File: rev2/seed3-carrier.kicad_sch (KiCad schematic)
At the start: 48 parts, among them J1 AudioJack2_Switch, J2 AudioJack2, J3 5V_IN, J4 DISPLAY_UART, J5 SJ1-3535NG, J6 Seed3_PINS_RIGHT, J7 Seed3_PINS_LEFT, Q1 AO3401A, U1 TLV9062IDR, U2 TPA6111A2DR

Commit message: Replace rev 2 pots with a volume encoder and add a watchdog output mute
- Remove RV1-RV3, C10, C11. R17 (1M to VREF) keeps the guitar input load;
  input trim and tone move to firmware.
- Add SW1 rotary encoder with push switch and RC conditioning on ENC_A/B/SW
  (Daisy pins 22/23/24).
- Add U3 (SN74LVC1G123) + Q2: U2 SHUTDOWN is pulled to +5V (muted) unless the
  firmware toggles AUDIO_ALIVE (pin 33) every audio callback; ~10 ms timeout.
- Add rev2/CHANGES.md listing these changes, firmware impact and open items.

Co-Authored-By: Claude Opus 5.5 <noreply@anthropic.com>
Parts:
- removed C10, C11: 100nF, Capacitor_SMD:C_1206_3216Metric_Pad1.33x1.80mm_HandSolder, symbol Device:C_Small
- removed RV1: 1M INPUT LEVEL, Seed3_Carrier:Potentiometer_Bourns_PTV09A-4_Single_Vertical_3mmMount, symbol Device:R_Potentiometer_Small
- removed RV2, RV3: 10k linear, Seed3_Carrier:Potentiometer_Bourns_PTV09A-4_Single_Vertical_3mmMount, symbol Device:R_Potentiometer_Small
- added C19, C20, C21: 10nF, Capacitor_SMD:C_1206_3216Metric_Pad1.33x1.80mm_HandSolder, symbol Device:C_Small
- added C22, C23: 100nF, Capacitor_SMD:C_1206_3216Metric_Pad1.33x1.80mm_HandSolder, symbol Device:C_Small
- added Q2: 2N7002, Package_TO_SOT_SMD:SOT-23, symbol Transistor_FET:2N7002
- added R17: 1M, Resistor_SMD:R_1206_3216Metric_Pad1.30x1.75mm_HandSolder, symbol Device:R_Small_US
- added R18, R19, R20, R21, R22, R23: 10k, Resistor_SMD:R_1206_3216Metric_Pad1.30x1.75mm_HandSolder, symbol Device:R_Small_US
- added R24, R25, R26, R27: 100k, Resistor_SMD:R_1206_3216Metric_Pad1.30x1.75mm_HandSolder, symbol Device:R_Small_US
- added SW1: EC11E, Rotary_Encoder:RotaryEncoder_Alps_EC11E-Switch_Vertical_H20mm, symbol Device:RotaryEncoder_Switch
- added TP10: TP_SHDN, TestPoint:TestPoint_Pad_D2.0mm, symbol Connector:TestPoint
- added U3: SN74LVC1G123DCTR, Package_SO:SSOP-8_2.95x2.8mm_P0.65mm, symbol 74xGxx:74LVC1G123
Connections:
- net +5V: now also R27.1
- net 3V3_D: now also C23.1, R18.1, R20.1, R22.1, R24.1, U3.3 (~{CLR}), U3.8 (VCC)
- net GND: now also C19.2, C20.2, C21.2, C23.2, Q2.2 (S), R25.2, R26.2, SW1.C, SW1.S1, U3.1 (~{A}), U3.4 (GND); no longer U2.5 (SHDN)
- net VREF: now also R17.2
- net at R1.1: now also C3.2, R17.1
- net A2 renamed ENC_SW
- net ENC_SW: now also C21.1, R23.2
- net D26 renamed AUDIO_ALIVE
- net AUDIO_ALIVE: now also R25.1, U3.2 (B)
- net TONE_POT renamed ENC_B
- net ENC_B: now also C20.1, R21.2
- net VOLUME_POT renamed ENC_A
- net ENC_A: now also C19.1, R19.2
- new net: C22.1, U3.6 (Cext)
- new net: C22.2, R24.2, U3.7 (RCext)
- new net: Q2.1 (G), R26.1, U3.5 (Q)
- new net AMP_SHUTDOWN: Q2.3 (D), R27.2, TP10.1, U2.5 (SHDN)
- new net ENC_A_RAW: R18.2, R19.1, SW1.A
- new net ENC_B_RAW: R20.2, R21.1, SW1.B
- new net ENC_SW_RAW: R22.2, R23.1, SW1.S2
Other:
- note added: "Amps stay muted (SHUTDOWN pulled to +5V) unless the firmware toggles AUDIO_ALIVE from the audio callback. Each rising edge retriggers U3; if edges stop for ~10 ms (Rext x Cext), Q falls, Q2 turns off and the amps mute. Also muted while the Daisy is absent, booting or in DFU (B is held low). Wire the rev 2 speaker amp mute to AMP_SHUTDOWN."
- note added: "Master volume: rotary encoder, push = mute. 10k pull-up, 10k series, 10nF per encoder vendor app notes."
- note added: "OUTPUT MUTE WATCHDOG"
- note added: "R17 = 1M guitar input load. No input level pot: trim gain in firmware."
- note removed: "RV1: CW = full level. Turn down for hot pickups/pedals."

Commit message: Feed the speaker from AUDIO_OUT_2 and detect headphones in firmware
- Drop the J5 tip-switch line out; TN/RN are now no-connects.
- Add AUDIO_OUT_2 -> RC filter -> U1C buffer -> C26 -> LINE_SEND -> J2.
- Swap U1 to a TLV9064 quad (SOIC-14); U1D parked as a VREF follower for
  the future AUX input buffer.
- Add HP_DETECT on Daisy pin 34 (was D27) with pull-up, series R, filter
  cap and TP11; J5 still needs a jack with an isolated detect switch.
- Update rev2/CHANGES.md.

Co-Authored-By: Claude Opus 5.5 <noreply@anthropic.com>
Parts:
- added C24: 1nF, Capacitor_SMD:C_1206_3216Metric_Pad1.33x1.80mm_HandSolder, symbol Device:C_Small
- added C25: 1uF, Capacitor_SMD:C_1206_3216Metric_Pad1.33x1.80mm_HandSolder, symbol Device:C_Small
- added C26: 10uF, Capacitor_SMD:C_1206_3216Metric_Pad1.33x1.80mm_HandSolder, symbol Device:C_Small
- added C27: 100nF, Capacitor_SMD:C_1206_3216Metric_Pad1.33x1.80mm_HandSolder, symbol Device:C_Small
- added R28: 3.3k, Resistor_SMD:R_1206_3216Metric_Pad1.30x1.75mm_HandSolder, symbol Device:R_Small_US
- added R29: 1M, Resistor_SMD:R_1206_3216Metric_Pad1.30x1.75mm_HandSolder, symbol Device:R_Small_US
- added R30: 10k, Resistor_SMD:R_1206_3216Metric_Pad1.30x1.75mm_HandSolder, symbol Device:R_Small_US
- added R31: 1k, Resistor_SMD:R_1206_3216Metric_Pad1.30x1.75mm_HandSolder, symbol Device:R_Small_US
- added TP11: TP_HP_DET, TestPoint:TestPoint_Pad_D2.0mm, symbol Connector:TestPoint
- added unit 4 of U1
- added unit 3 of U1
- U1: value TLV9062IDR -> TLV9064IDR; footprint Package_SO:SOIC-8_3.9x4.9mm_P1.27mm -> Package_SO:SOIC-14_3.9x8.7mm_P1.27mm; symbol Amplifier_Operational:TL072 -> Amplifier_Operational:TL074
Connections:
- net +5V: now also U1.4 (V+); no longer U1.8 (V+)
- net 3V3_D: now also R30.1
- net AUDIO_OUT_2: now also R28.1
- net GND: now also U1.11 (V-), C24.2, C27.2; no longer U1.4 (V-)
- net LINE_SEND: now also C26.2; no longer J5.TN
- net VREF: now also R29.1, U1.12 (+)
- net D27 renamed HP_DETECT
- net HP_DETECT: now also C27.1, R30.2, R31.2
- new net: U1.13 (-), U1.14
- new net: C24.1, C25.1, R28.2
- new net: C25.2, R29.2, U1.10 (+)
- new net: C26.1, U1.8, U1.9 (-)
- new net HP_DETECT_SW: R31.1, TP11.1
- no-connect marks 2 -> 3
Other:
- note added: "AUDIO_OUT_2 feeds the speaker amp / J2 independently of the headphones. Firmware sets its level and mutes it when HP_DETECT shows headphones are in. U1D is a spare, parked as a VREF follower: use it for the AUX input buffer."
- note added: "Headphone detect: J5 needs a jack with an isolated detect switch (part TBD). Wire it between HP_DETECT_SW and GND. Bring-up: short TP11 to GND to simulate headphones."
- note added: "SPEAKER / LINE SEND"
- note removed: "Line out: J2 is fed from HP_L through J5's tip switch (LINE_SEND). Plugging headphones into J5 mutes J2."

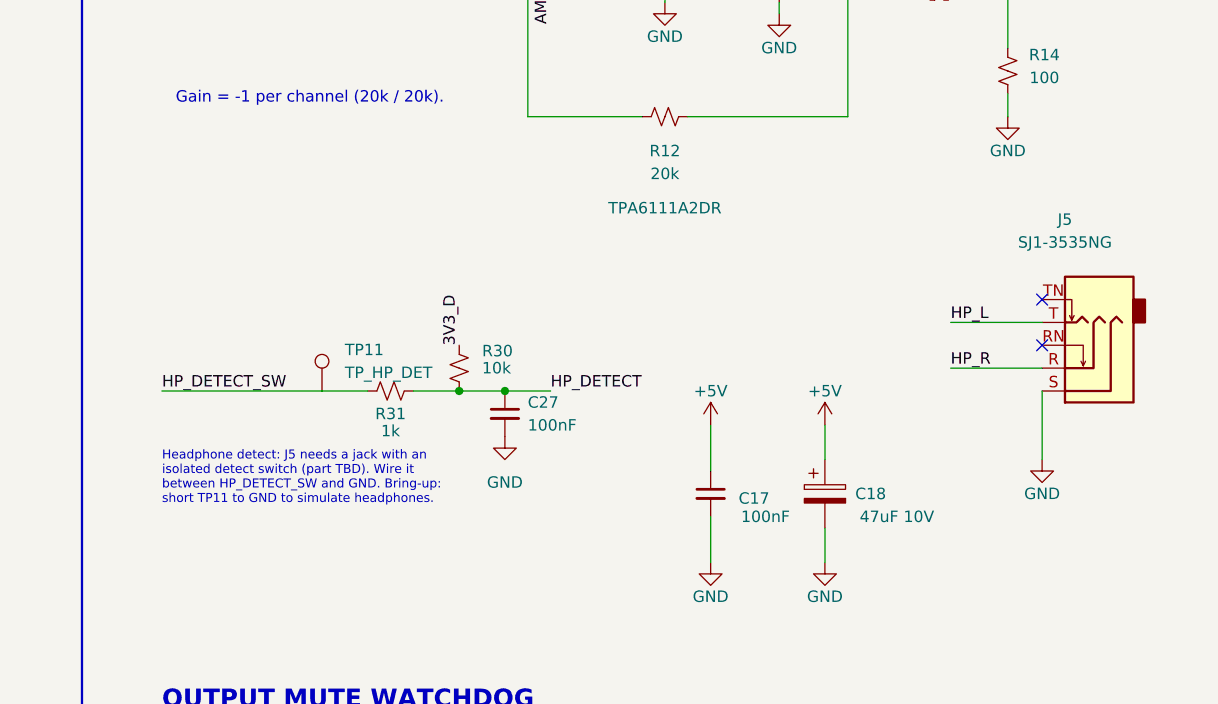
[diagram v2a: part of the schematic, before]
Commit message: Use SJ3-35063AG for J5 with an isolated headphone-detect switch
- Add SJ3-35063AG symbol (project library) and footprint (Seed3_Carrier),
  drawn from the Same Sky SJ3-3506X recommended PCB layout.
- Swap J5 in rev 2: tip/ring/sleeve unchanged; pin 5 to GND, pin 6 (N-O,
  closes on insertion) to HP_DETECT_SW, so HP_DETECT is low with
  headphones in.
- Update rev2/CHANGES.md.

Co-Authored-By: Claude Opus 5.5 <noreply@anthropic.com>
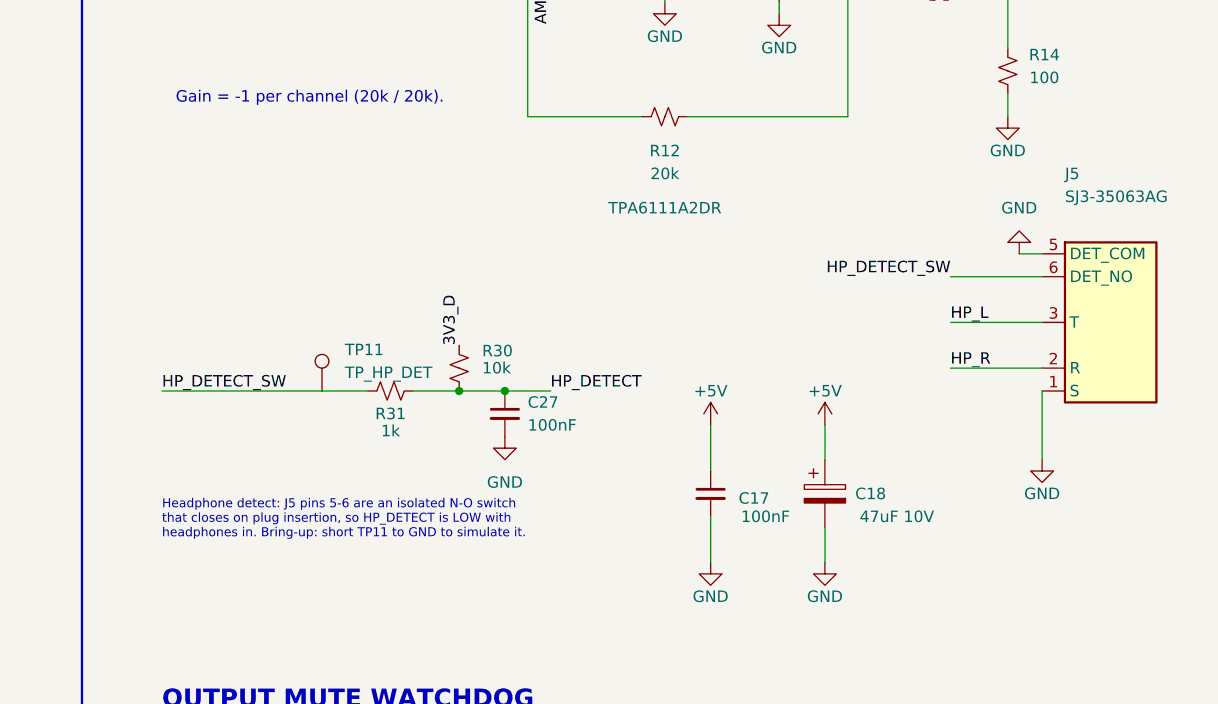
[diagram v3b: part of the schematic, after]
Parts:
- removed J5: SJ1-3535NG, Connector_Audio:Jack_3.5mm_CUI_SJ1-3535NG_Horizontal, symbol Connector_Audio:AudioJack3_SwitchTR
- added J5: SJ3-35063AG, Seed3_Carrier:Jack_3.5mm_SameSky_SJ3-35063AG_Horizontal, symbol seed3-carrier:SJ3-35063AG
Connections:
- net GND: now also J5.1 (S), J5.5 (DET_COM)
- net HP_DETECT_SW: now also J5.6 (DET_NO)
- net HP_L: now also J5.3 (T)
- net HP_R: now also J5.2 (R)
- no-connect marks 3 -> 1
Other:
- note added: "Headphone detect: J5 pins 5-6 are an isolated N-O switch that closes on plug insertion, so HP_DETECT is LOW with headphones in. Bring-up: short TP11 to GND to simulate it."
- note removed: "Headphone detect: J5 needs a jack with an isolated detect switch (part TBD). Wire it between HP_DETECT_SW and GND. Bring-up: short TP11 to GND to simulate headphones."
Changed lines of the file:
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@@
 		(at 45.72 43.18)
 	)
-	(no_connect
-		(at 387.35 116.84)
-	)
 	(wire
 		(pts
@@
 	)
 	(symbol
-		(lib_id "Connector_Audio:AudioJack3_SwitchTR")
-		(at 392.43 119.38 180)
-		(unit 1)
-		(body_style 1)
-		(exclude_from_sim no)
-		(in_bom yes)
-		(on_board yes)
-		(in_pos_files yes)
-		(dnp no)
-		(property "Reference" "J5"
-			(at 389.89 102.87 0)
-			(show_name no)
-			(do_not_autoplace no)
-			(effects
-				(font
-					(size 1.27 1.27)
-				)
-			)
-		)
-		(property "Value" "SJ1-3535NG"
-			(at 389.89 105.41 0)
-			(show_name no)
-			(do_not_autoplace no)
-			(effects
-				(font
-					(size 1.27 1.27)
-				)
-			)
-		)
-		(property "Footprint" "Connector_Audio:Jack_3.5mm_CUI_SJ1-3535NG_Horizontal"
-			(at 392.43 119.38 0)
-			(hide yes)
-			(show_name no)
-			(do_not_autoplace no)
-			(effects
-				(font
-					(size 1.27 1.27)
-				)
-			)
-		)
-		(property "Datasheet" ""
-			(at 392.43 119.38 0)
-			(show_name no)
-			(do_not_autoplace no)
-			(effects
-				(font
-					(size 1.27 1.27)
-				)
-			)
-		)
-		(property "Description" ""
-			(at 392.43 119.38 0)
-			(show_name no)
-			(do_not_autoplace no)
-			(effects
-				(font
-					(size 1.27 1.27)
-				)
-			)
-		)
-		(pin "R"
-		)
-		(pin "S"
-		)
-		(pin "T"
-		)
-		(pin "TN"
-		)
-		(pin "RN"
-		)
-		(instances
-			(project "seed3-carrier"
-				(path "/94ecceca-f8ce-4e68-9c84-99ac5115dfb9"
-					(reference "J5")
-					(unit 1)
-				)
-			)
-		)
-	)
-	(symbol
 		(lib_id "Device:R_Small_US")
 		(at 345.44 91.44 90)
@@
 		)
 	)
-	(no_connect
-		(at 387.35 111.76)
-	)
 	(text "SPEAKER / LINE SEND"
 		(exclude_from_sim no)
@@
 		)
 	)
-	(text "Headphone detect: J5 needs a jack with an\nisolated detect switch (part TBD). Wire it\nbetween HP_DETECT_SW and GND. Bring-up:\nshort TP11 to GND to simulate headphones."
+	(symbol
+		(lib_id "seed3-carrier:SJ3-35063AG")
+		(at 392.43 119.38 0)
+		(unit 1)
+		(body_style 1)
+		(exclude_from_sim no)
+		(in_bom yes)
+		(on_board yes)
+		(in_pos_files yes)
+		(dnp no)
+		(property "Reference" "J5"
+			(at 389.89 97.79 0)
+			(show_name no)
+			(do_not_autoplace no)
+			(effects
+				(font
+					(size 1.27 1.27)
+				)
+				(justify left)
+			)
+		)
+		(property "Value" "SJ3-35063AG"
+			(at 389.89 100.33 0)
+			(show_name no)
+			(do_not_autoplace no)
+			(effects
+				(font
+					(size 1.27 1.27)
+				)
+				(justify left)
+			)
+		)
+		(property "Footprint" "Seed3_Carrier:Jack_3.5mm_SameSky_SJ3-35063AG_Horizontal"
+			(at 392.43 119.38 0)
+			(hide yes)
+			(show_name no)
+			(do_not_autoplace no)
+			(effects
+				(font
+					(size 1.27 1.27)
+				)
+			)
+		)
+		(property "Datasheet" "https://www.sameskydevices.com/product/resource/sj3-3506x.pdf"
+			(at 392.43 119.38 0)
+			(hide yes)
+			(show_name no)
+			(do_not_autoplace no)
+			(effects
+				(font
+					(size 1.27 1.27)
+				)
+			)
+		)
+		(property "Description" "3.5mm stereo (TRS) jack, through hole, with isolated normally-open detect switch"
+			(at 392.43 119.38 0)
+			(hide yes)
+			(show_name no)
+			(do_not_autoplace no)
+			(effects
+				(font
+					(size 1.27 1.27)
+				)
+			)
+		)
+		(pin "5"
+		)
+		(pin "6"
+		)
+		(pin "3"
+		)
+		(pin "2"
+		)
+		(pin "1"
+		)
+		(instances
+			(project "seed3-carrier"
+				(path "/94ecceca-f8ce-4e68-9c84-99ac5115dfb9"
+					(reference "J5")
+					(unit 1)
+				)
+			)
+		)
+	)
+	(wire
+		(pts
+			(xy 387.35 106.68) (xy 384.81 106.68)
+		)
+		(stroke
+			(width 0)
+			(type default)
+		)
+	)
+	(symbol
+		(lib_id "power:GND")
+		(at 384.81 106.68 180)
+		(unit 1)
+		(body_style 1)
+		(exclude_from_sim no)
+		(in_bom yes)
+		(on_board yes)
+		(in_pos_files yes)
+		(dnp no)
+		(property "Reference" "#PWR050"
+			(at 384.81 106.68 0)
+			(hide yes)
+			(show_name no)
+			(do_not_autoplace no)
+			(effects
+				(font
+					(size 1.27 1.27)
+				)
+			)
+		)
+		(property "Value" "GND"
+			(at 384.81 101.6 0)
+			(show_name no)
+			(do_not_autoplace no)
+			(effects
+				(font
+					(size 1.27 1.27)
+				)
+			)
+		)
+		(property "Footprint" ""
+			(at 384.81 106.68 0)
+			(hide yes)
+			(show_name no)
+			(do_not_autoplace no)
+			(effects
+				(font
+					(size 1.27 1.27)
+				)
+			)
+		)
+		(property "Datasheet" ""
+			(at 384.81 106.68 0)
+			(hide yes)
+			(show_name no)
+			(do_not_autoplace no)
+			(effects
+				(font
+					(size 1.27 1.27)
+				)
+			)
+		)
+		(property "Description" "Power symbol creates a global label with name \"GND\" , ground"
+			(at 384.81 106.68 0)
+			(hide yes)
+			(show_name no)
+			(do_not_autoplace no)
+			(effects
+				(font
+					(size 1.27 1.27)
+				)
+			)
+		)
+		(pin "1"
+		)
+		(instances
+			(project "seed3-carrier"
+				(path "/94ecceca-f8ce-4e68-9c84-99ac5115dfb9"
+					(reference "#PWR050")
+					(unit 1)
+				)
+			)
+		)
+	)
+	(wire
+		(pts
+			(xy 387.35 109.22) (xy 377.19 109.22)
+		)
+		(stroke
+			(width 0)
+			(type default)
+		)
+	)
+	(label "HP_DETECT_SW"
+		(at 377.19 109.22 180)
+		(effects
+			(font
+				(size 1.27 1.27)
+			)
+			(justify right bottom)
+		)
+	)
+	(text "Headphone detect: J5 pins 5-6 are an isolated N-O switch\nthat closes on plug insertion, so HP_DETECT is LOW with\nheadphones in. Bring-up: short TP11 to GND to simulate it."
 		(exclude_from_sim no)
-		(at 289.56 134.62 0)
+		(at 289.56 138.43 0)
 		(effects
 			(font

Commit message: Replace J3 with an 8-pin JST-XH power board connector
- J3 is now a JST-XH B8B-XH-A carrying 5V (pins 1-2), GND (3-4),
  BATT_SENSE, PWR_BTN, PWR_HOLD and SPK_MUTE (5-8). Q1 stays as
  reverse-polarity protection on the new 5V_IN net.
- Daisy pins 25-28 (A3-A6) become BATT_SENSE, PWR_BTN, PWR_HOLD and
  SPK_EN, also renamed on the J7 breakout. Add R32-R36, C28, C29 for
  filtering, pull-up and pull-down.
- Add Q3/Q4 in series so SPK_MUTE only unmutes the speaker amp when
  the watchdog (U3 Q, now named WD_OK) and SPK_EN are both high.
  AMP_SHUTDOWN now mutes only the headphone amp.
- Feed the display through FB1 and C30 (J4 pin 4 is now DISPLAY_5V).
- Update rev2/CHANGES.md with the pin map, power board requirements,
  firmware changes and open items.

Co-Authored-By: Claude Opus 5.5 <noreply@anthropic.com>
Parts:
- added C28, C29: 100nF, Capacitor_SMD:C_1206_3216Metric_Pad1.33x1.80mm_HandSolder, symbol Device:C_Small
- added C30: 47uF, Capacitor_SMD:C_1210_3225Metric_Pad1.33x2.70mm_HandSolder, symbol Device:C_Small
- added FB1: 600R@100MHz, Inductor_SMD:L_1206_3216Metric_Pad1.22x1.90mm_HandSolder, symbol Device:FerriteBead_Small
- added Q3, Q4: 2N7002, Package_TO_SOT_SMD:SOT-23, symbol Transistor_FET:2N7002
- added R32, R33, R35: 1k, Resistor_SMD:R_1206_3216Metric_Pad1.30x1.75mm_HandSolder, symbol Device:R_Small_US
- added R34, R37: 100k, Resistor_SMD:R_1206_3216Metric_Pad1.30x1.75mm_HandSolder, symbol Device:R_Small_US
- added R36: 10k, Resistor_SMD:R_1206_3216Metric_Pad1.30x1.75mm_HandSolder, symbol Device:R_Small_US
- J3: value 5V_IN -> POWER_BOARD; footprint Connector_PinHeader_2.54mm:PinHeader_1x02_P2.54mm_Vertical -> Connector_JST:JST_XH_B8B-XH-A_1x08_P2.50mm_Vertical; symbol Connector_Generic:Conn_01x02 -> Connector_Generic:Conn_01x08
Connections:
- net +5V: now also FB1.1; no longer J4.4 (Pin_4)
- net 3V3_D: now also R36.1
- net GND: now also J3.3 (Pin_3), J3.4 (Pin_4), C28.2, C29.2, C30.2, Q4.2 (S), R34.2, R37.2; no longer J3.2 (Pin_2)
- net 5V_IN: now reaches J3.1 (Pin_1), Q1.3 (D)
- net 5V_IN: now also J3.2 (Pin_2)
- net WD_OK: now reaches Q2.1 (G), R26.1, U3.5 (Q)
- net WD_OK: now also Q3.1 (G)
- net A3 renamed BATT_SENSE
- net BATT_SENSE: now also C28.1, R32.2
- net A4 renamed PWR_BTN
- net PWR_BTN: now also C29.1, R35.2, R36.2
- net A5 renamed PWR_HOLD
- net PWR_HOLD: now also R33.1
- net A6 renamed SPK_EN
- net SPK_EN: now also Q4.1 (G), R37.1
- new net: Q3.2 (S), Q4.3 (D)
- new net BATT_SENSE_CONN: J3.5 (Pin_5), R32.1
- new net DISPLAY_5V: C30.1, FB1.2, J4.4 (Pin_4)
- new net PWR_BTN_CONN: J3.6 (Pin_6), R35.1
- new net PWR_HOLD_CONN: J3.7 (Pin_7), R33.2, R34.1
- new net SPK_MUTE: J3.8 (Pin_8), Q3.3 (D)
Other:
- note added: "J3 goes to the power board (JST-XH, 8 pins). Pins 5-7 are 3.3 V logic: nothing above 3.3 V on them. SPK_MUTE is open drain. The power board pulls it up, so the speaker amp stays muted unless WD_OK and SPK_EN are both high."
- note added: "POWER BOARD CONNECTOR"
- note added: "U2 stays muted (SHUTDOWN pulled to +5V) unless the firmware toggles AUDIO_ALIVE from the audio callback. Each rising edge retriggers U3; if edges stop for ~10 ms (Rext x Cext), Q falls, Q2 turns off and the amps mute. Also muted while the Daisy is absent, booting or in DFU (B is held low). AMP_SHUTDOWN mutes U2; the speaker amp uses SPK_MUTE on J3."
- note removed: "Amps stay muted (SHUTDOWN pulled to +5V) unless the firmware toggles AUDIO_ALIVE from the audio callback. Each rising edge retriggers U3; if edges stop for ~10 ms (Rext x Cext), Q falls, Q2 turns off and the amps mute. Also muted while the Daisy is absent, booting or in DFU (B is held low). Wire the rev 2 speaker amp mute to AMP_SHUTDOWN."
